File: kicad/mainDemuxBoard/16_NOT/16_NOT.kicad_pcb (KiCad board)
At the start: 4 copper layers, 32 parts, among them Q1194 NMOS, Q1196 NMOS, Q1198 NMOS, Q1200 NMOS, Q1202 NMOS, Q1204 NMOS, Q1206 NMOS, Q1208 NMOS, Q1210 NMOS, Q1212 NMOS, Q1214 NMOS, Q1216 NMOS, Q1218 NMOS, Q1220 NMOS, Q1222 NMOS, Q1224 NMOS

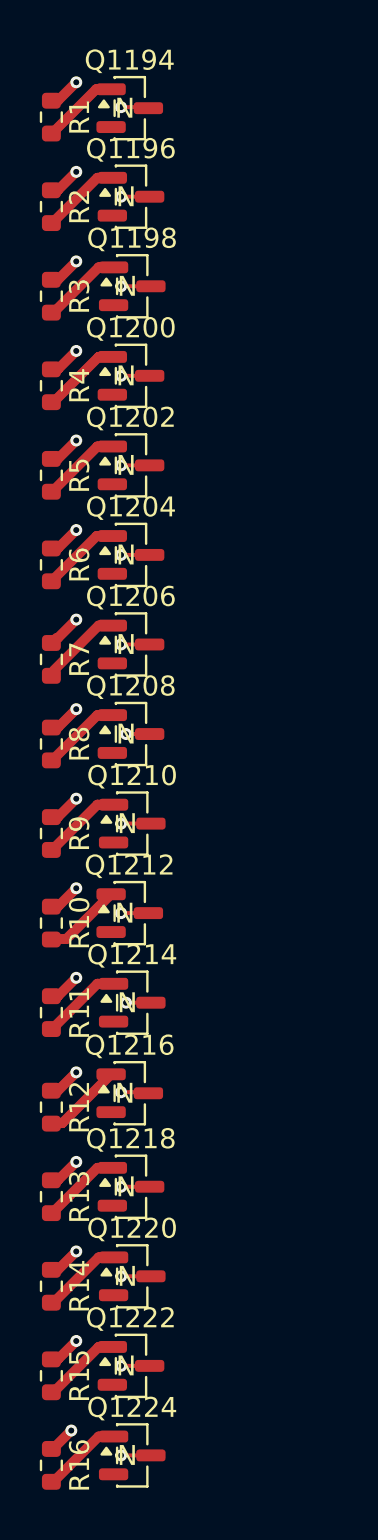
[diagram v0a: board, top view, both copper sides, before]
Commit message: update main board schematic
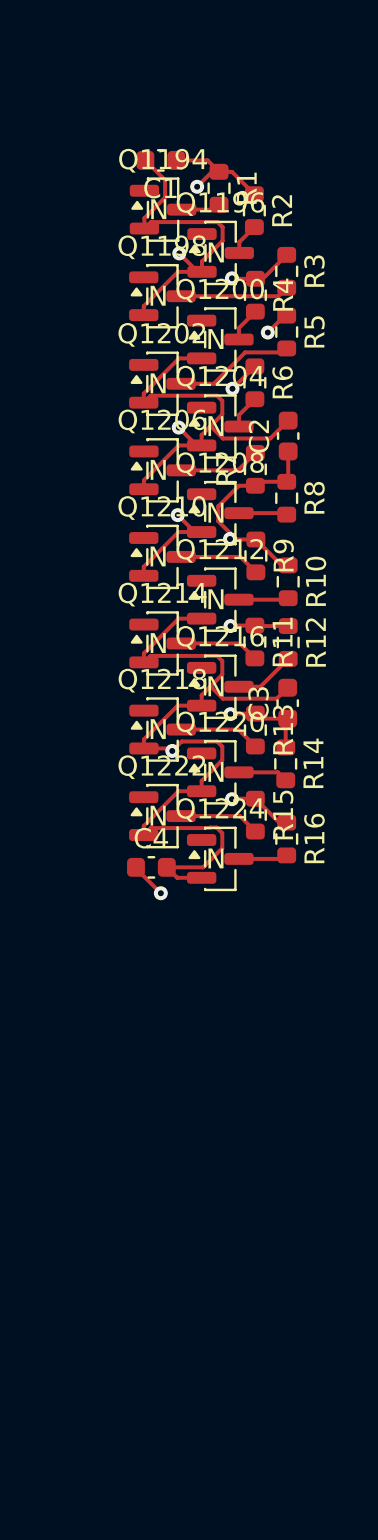
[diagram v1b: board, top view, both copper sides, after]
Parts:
- added C1: 100nC, Capacitor_SMD:C_0603_1608Metric, F.Cu at (91.5, 53.7)
- added C2: 100nC, Capacitor_SMD:C_0603_1608Metric, F.Cu at (97.9, 67.5)
- added C3: 100nC, Capacitor_SMD:C_0603_1608Metric, F.Cu at (97.9, 81.0)
- added C4: 100nC, Capacitor_SMD:C_0603_1608Metric, F.Cu at (91.0, 89.2)
- Q1194, Q1196, Q1198, Q1200, Q1202, Q1204, Q1206, Q1208, Q1210, Q1212, Q1214, Q1216, Q1218, Q1220, Q1222, Q1224: value NMOS -> Q_NMOS_GSD
- moved R16 33.6 mm to (97.8, 87.8)
- moved Q1224 30.3 mm to (94.6, 88.8)
- moved R15 30.0 mm to (96.2, 86.6)
- moved R14 28.8 mm to (97.8, 84.0)
- moved Q1222 27.7 mm to (91.7, 86.6)
- moved R12 26.2 mm to (97.9, 77.9)
- moved Q1220 25.7 mm to (94.6, 84.4)
- moved R13 25.6 mm to (96.2, 82.3)
- moved Q1218 23.0 mm to (91.7, 82.3)
- moved R11 21.2 mm to (96.2, 77.9)
- moved Q1216 20.9 mm to (94.6, 80.1)
- moved R10 20.9 mm to (97.9, 74.8)
- moved Q1214 18.1 mm to (91.7, 78.0)
- moved R9 17.3 mm to (96.3, 73.5)
- moved R8 17.1 mm to (97.8, 70.7)
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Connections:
- Q1194 pad 1: /~{Y_{0}} -> /A_{0}
- Q1194 pad 2: /A_{0} -> GND
- Q1194 pad 3: GND -> /~{Y_{0}}
- Q1196 pad 1: /~{Y_{1}} -> /A_{1}
- Q1196 pad 2: /A_{1} -> GND
- Q1196 pad 3: GND -> /~{Y_{1}}
- Q1198 pad 1: /~{Y_{2}} -> /A_{2}
- Q1198 pad 2: /A_{2} -> GND
- Q1198 pad 3: GND -> /~{Y_{2}}
- Q1200 pad 1: /~{Y_{3}} -> /A_{3}
- Q1200 pad 2: /A_{3} -> GND
- Q1200 pad 3: GND -> /~{Y_{3}}
- Q1202 pad 1: /~{Y_{4}} -> /A_{4}
- Q1202 pad 2: /A_{4} -> GND
- Q1202 pad 3: GND -> /~{Y_{4}}
- Q1204 pad 1: /~{Y_{5}} -> /A_{5}
- Q1204 pad 2: /A_{5} -> GND
- Q1204 pad 3: GND -> /~{Y_{5}}
- Q1206 pad 1: /~{Y_{6}} -> /A_{6}
- Q1206 pad 2: /A_{6} -> GND
- Q1206 pad 3: GND -> /~{Y_{6}}
- Q1208 pad 1: /~{Y_{7}} -> /A_{7}
- Q1208 pad 2: /A_{7} -> GND
- Q1208 pad 3: GND -> /~{Y_{7}}
- Q1210 pad 1: /~{Y_{8}} -> /A_{8}
- Q1210 pad 2: /A_{8} -> GND
- Q1210 pad 3: GND -> /~{Y_{8}}
- Q1212 pad 1: /~{Y_{9}} -> /A_{9}
- Q1212 pad 2: /A_{9} -> GND
- Q1212 pad 3: GND -> /~{Y_{9}}
- Q1214 pad 1: /~{Y_{10}} -> /A_{10}
- Q1214 pad 2: /A_{10} -> GND
- Q1214 pad 3: GND -> /~{Y_{10}}
- Q1216 pad 1: /~{Y_{11}} -> /A_{11}
- Q1216 pad 2: /A_{11} -> GND
- Q1216 pad 3: GND -> /~{Y_{11}}
- Q1218 pad 1: /~{Y_{12}} -> /A_{12}
- Q1218 pad 2: /A_{12} -> GND
- Q1218 pad 3: GND -> /~{Y_{12}}
- Q1220 pad 1: /~{Y_{13}} -> /A_{13}
- Q1220 pad 2: /A_{13} -> GND
- Q1220 pad 3: GND -> /~{Y_{13}}
- Q1222 pad 1: /~{Y_{14}} -> /A_{14}
- Q1222 pad 2: /A_{14} -> GND
- Q1222 pad 3: GND -> /~{Y_{14}}
- Q1224 pad 1: /~{Y_{15}} -> /A_{15}
- Q1224 pad 2: /A_{15} -> GND
- Q1224 pad 3: GND -> /~{Y_{15}}
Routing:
- net GND: track 24.0 -> 84.0 mm, vias 16 -> 4
- net +5V: track 22.1 -> 35.7 mm, vias 16 -> 9
- net /~{Y_{1}}: track 3.93 -> 1.61 mm
- net /~{Y_{5}}: track 4.00 -> 1.71 mm
- net /~{Y_{3}}: track 3.87 -> 1.74 mm
- net /~{Y_{4}}: track 3.93 -> 6.04 mm
- net /~{Y_{0}}: track 3.93 -> 1.98 mm
- net /~{Y_{2}}: track 3.93 -> 5.48 mm
- net /~{Y_{7}}: track 3.93 -> 2.43 mm
- net /~{Y_{15}}: track 3.93 -> 2.47 mm
- net /~{Y_{13}}: track 3.93 -> 2.52 mm
- net /~{Y_{9}}: track 3.81 -> 2.51 mm
- net /~{Y_{11}}: track 4.01 -> 3.05 mm
